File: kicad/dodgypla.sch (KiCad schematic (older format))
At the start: 10 parts, among them J1 PLA_Conn, J2 PAD_TCK, J3 PAD_TMS, J4 PAD_TDO, J5 PAD_TDI, U1 AMS1117, U2 XC9536XL-10VQ44C

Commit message: Converting to two-layer board for PCB manufacturing.
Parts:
- C1, C2, C3: symbol C -> device:C
- J1: symbol Conn_02x14_Counter_Clockwise -> conn:Conn_02x14_Counter_Clockwise
- J2, J3, J4, J5: symbol Conn_01x01 -> conn:Conn_01x01
- U1: footprint TO_SOT_Packages_SMD:SOT-223-3Lead_TabPin2 -> TO_SOT_Packages_SMD:SOT-223-3_TabPin2; symbol AMS1117 -> ams1117:AMS1117
- U2: symbol XC9536XL-10VQ44C -> xc9536xl-10vq44c:XC9536XL-10VQ44C
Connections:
- wire segments 14 -> 22
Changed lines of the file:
@@
-EESchema Schematic File Version 2
-LIBS:power
-LIBS:device
-LIBS:switches
-LIBS:relays
-LIBS:motors
-LIBS:transistors
-LIBS:conn
-LIBS:linear
-LIBS:regul
-LIBS:74xx
-LIBS:cmos4000
-LIBS:adc-dac
-LIBS:memory
-LIBS:xilinx
-LIBS:microcontrollers
-LIBS:dsp
-LIBS:microchip
-LIBS:analog_switches
-LIBS:motorola
-LIBS:texas
-LIBS:intel
-LIBS:audio
-LIBS:interface
-LIBS:digital-audio
-LIBS:philips
-LIBS:display
-LIBS:cypress
-LIBS:siliconi
-LIBS:opto
-LIBS:atmel
-LIBS:contrib
-LIBS:valves
-LIBS:xc9536xl-10vq44c
-LIBS:ams1117
+EESchema Schematic File Version 4
 LIBS:dodgypla-cache
-EELAYER 25 0
+EELAYER 29 0
 EELAYER END
 $Descr A4 11693 8268
@@
 Title "DodgyPLA"
 Date ""
-Rev "1"
+Rev "2"
 Comp ""
 Comment1 "Commodore 64 PLA Replacement"
-Comment2 "http://github.com/desaster/c64-dodgypla"
-Comment3 ""
+Comment2 "Heavily based on: http://github.com/desaster/c64-dodgypla"
+Comment3 "http://github.com/hackup/c64-dodgypla"
 Comment4 ""
 $EndDescr
 $Comp
-L Conn_02x14_Counter_Clockwise J1
+L conn:Conn_02x14_Counter_Clockwise J1
 U 1 1 5A0C74B0
 P 2100 4600
@@
 	2900 4000 2900 3750
 $Comp
-L +5V #PWR01
+L power:+5V #PWR01
 U 1 1 5A0C762B
 P 2900 3750
@@
 	1500 5300 1500 5700
 $Comp
-L GND #PWR02
+L power:GND #PWR02
 U 1 1 5A0C7674
 P 1500 5700
@@
 PLA_FE
 $Comp
-L Conn_01x01 J2
+L conn:Conn_01x01 J2
 U 1 1 5A0C7874
 P 10750 5300
@@
 $EndComp
 $Comp
-L Conn_01x01 J3
+L conn:Conn_01x01 J3
 U 1 1 5A0C793C
 P 10750 5600
@@
 $EndComp
 $Comp
-L Conn_01x01 J4
+L conn:Conn_01x01 J4
 U 1 1 5A0C797A
 P 10750 5900
@@
 $EndComp
 $Comp
-L Conn_01x01 J5
+L conn:Conn_01x01 J5
 U 1 1 5A0C7AB0
 P 10750 6200
@@
 	11000 4950 11000 6400
 $Comp
-L +3.3V #PWR03
+L power:+3.3V #PWR03
 U 1 1 5A0C804E
 P 3150 900
@@
 $EndComp
 $Comp
-L +5V #PWR04
+L power:+5V #PWR04
 U 1 1 5A0C80E4
 P 750 900
@@
 $EndComp
 $Comp
-L C C1
+L device:C C1
 U 1 1 5A0C8111
 P 1050 1050
@@
 $EndComp
 $Comp
-L GND #PWR05
+L power:GND #PWR05
 U 1 1 5A0C820D
 P 750 1450
@@
 $EndComp
 $Comp
-L C C2
+L device:C C2
 U 1 1 5A0C8072
 P 2850 1050
@@
 JTAG_TCK
 $Comp
-L C C3
+L device:C C3
 U 1 1 5A0C905D
 P 9600 2750
@@
 $EndComp
 $Comp
-L GND #PWR06
+L power:GND #PWR06
 U 1 1 5A0C90C1
 P 9600 2900
@@
 PLA_VA13
 $Comp
-L GND #PWR07
+L power:GND #PWR07
 U 1 1 5A0CABE7
 P 5450 5150
@@
 Only 1 bypass cap due\nto space constraints
 Wire Wire Line
-	750  900  1150 900
+	750  900  1050 900
 Connection ~ 1050 900
 Wire Wire Line
-	2750 900  3150 900
+	2750 900  2850 900
 Connection ~ 2850 900
 Wire Wire Line
 	2850 1400 2850 1200
 Wire Wire Line
-	750  1400 2850 1400
+	750  1400 1050 1400
 Wire Wire Line
 	750  1400 750  1450
@@
 Connection ~ 1050 1400
 $Comp
-L +5V #PWR08
+L power:+5V #PWR08
 U 1 1 5A0CBA4B
 P 1500 2000
@@
 $EndComp
 $Comp
-L PWR_FLAG #FLG09
+L power:PWR_FLAG #FLG09
 U 1 1 5A0CBA6C
 P 1500 2000
@@
 $EndComp
 $Comp
-L +3.3V #PWR010
+L power:+3.3V #PWR010
 U 1 1 5A0C9098
 P 9600 2600
@@
 $EndComp
 $Comp
-L GND #PWR011
+L power:GND #PWR011
 U 1 1 5A0CBEB0
 P 2000 2000
@@
 $EndComp
 $Comp
-L PWR_FLAG #FLG012
+L power:PWR_FLAG #FLG012
 U 1 1 5A0CBEE3
 P 2000 2000
@@
 $EndComp
 $Comp
-L XC9536XL-10VQ44C U2
+L xc9536xl-10vq44c:XC9536XL-10VQ44C U2
 U 1 1 5A6F8821
 P 5850 3600
@@
 NoConn ~ 4850 3300
 $Comp
-L +3V3 #PWR013
+L power:+3V3 #PWR013
 U 1 1 5A6F9301
 P 6300 2300
@@
 $EndComp
 Wire Wire Line
-	5650 2400 6300 2400
+	5650 2400 5850 2400
 Wire Wire Line
 	6300 2400 6300 2300
 Wire Wire Line
-	5450 5050 6050 5050
+	5450 5050 5650 5050
 Wire Wire Line
 	5450 5050 5450 5150
@@
 NoConn ~ 6850 2900
 $Comp
-L AMS1117 U1
+L ams1117:AMS1117 U1
 U 1 1 5A6FA036
 P 1950 900
 F 0 "U1" H 2200 750 50  0000 C CNN
 F 1 "AMS1117" H 1700 1000 50  0000 C CNN
-F 2 "TO_SOT_Packages_SMD:SOT-223-3Lead_TabPin2" H 1950 900 60  0001 C CNN
+F 2 "TO_SOT_Packages_SMD:SOT-223-3_TabPin2" H 1950 900 60  0001 C CNN
 F 3 "" H 1950 900 60  0000 C CNN
 	1    1950 900
 	1    0    0    -1
 $EndComp
+Wire Wire Line
+	1050 900  1150 900
+Wire Wire Line
+	2850 900  3150 900
+Wire Wire Line
+	1950 1400 2850 1400
+Wire Wire Line
+	1050 1400 1950 1400
+Wire Wire Line
+	5850 5050 6050 5050
+Wire Wire Line
+	5650 5050 5850 5050
+Wire Wire Line
+	5850 2400 6050 2400
+Wire Wire Line
+	6050 2400 6300 2400
 $EndSCHEMATC

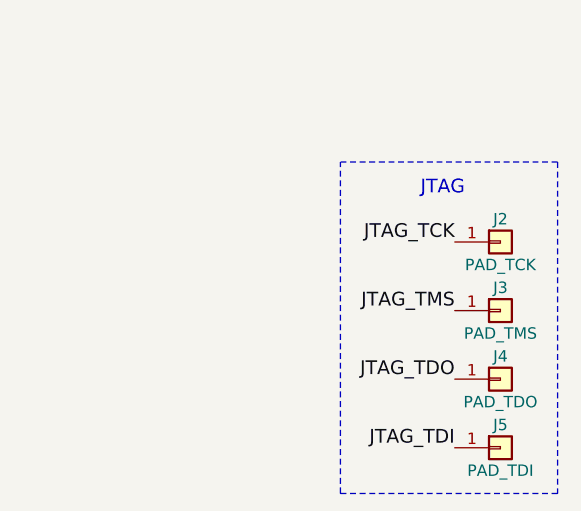
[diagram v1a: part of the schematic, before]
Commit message: Converting to two-layer board for PCB manufacturing.
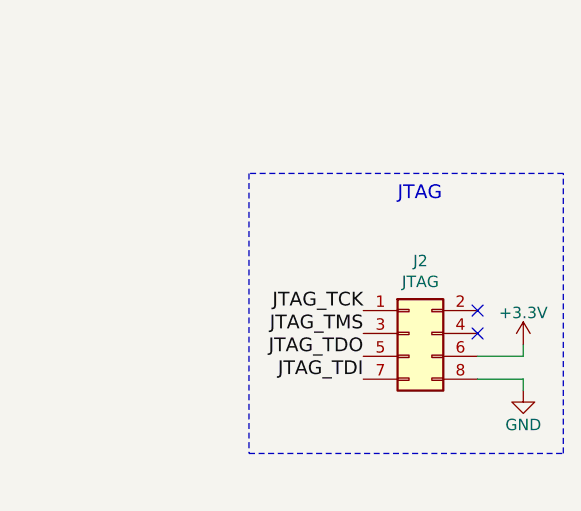
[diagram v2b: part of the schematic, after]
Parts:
- removed J2: PAD_TCK, dodgyPLA_footprints:testpad_1.6mm, symbol conn:Conn_01x01
- removed J3: PAD_TMS, dodgyPLA_footprints:testpad_1.6mm, symbol conn:Conn_01x01
- removed J4: PAD_TDO, dodgyPLA_footprints:testpad_1.6mm, symbol conn:Conn_01x01
- removed J5: PAD_TDI, dodgyPLA_footprints:testpad_1.6mm, symbol conn:Conn_01x01
- added J2: JTAG, Pin_Headers:Pin_Header_Straight_2x04_Pitch2.54mm, symbol conn:Conn_02x04_Odd_Even
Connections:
- net +3V3: now also J2.6 (Pin_6)
- net GND: now also J2.8 (Pin_8)
- net JTAG_TCK: now also J2.1 (Pin_1)
- net JTAG_TDI: now also J2.7 (Pin_7)
- net JTAG_TDO: now also J2.5 (Pin_5)
- net JTAG_TMS: now also J2.3 (Pin_3)
- no-connect marks 12 -> 14
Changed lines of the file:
@@
 Text Label 1900 4000 2    60   ~ 0
 PLA_FE
-$Comp
-L conn:Conn_01x01 J2
-U 1 1 5A0C7874
-P 10750 5300
-F 0 "J2" H 10750 5400 50  0000 C CNN
-F 1 "PAD_TCK" H 10750 5200 50  0000 C CNN
-F 2 "dodgyPLA_footprints:testpad_1.6mm" H 10750 5300 50  0001 C CNN
-F 3 "" H 10750 5300 50  0001 C CNN
-	1    10750 5300
-	1    0    0    -1
-$EndComp
-$Comp
-L conn:Conn_01x01 J3
-U 1 1 5A0C793C
-P 10750 5600
-F 0 "J3" H 10750 5700 50  0000 C CNN
-F 1 "PAD_TMS" H 10750 5500 50  0000 C CNN
-F 2 "dodgyPLA_footprints:testpad_1.6mm" H 10750 5600 50  0001 C CNN
-F 3 "" H 10750 5600 50  0001 C CNN
-	1    10750 5600
-	1    0    0    -1
-$EndComp
-$Comp
-L conn:Conn_01x01 J4
-U 1 1 5A0C797A
-P 10750 5900
-F 0 "J4" H 10750 6000 50  0000 C CNN
-F 1 "PAD_TDO" H 10750 5800 50  0000 C CNN
-F 2 "dodgyPLA_footprints:testpad_1.6mm" H 10750 5900 50  0001 C CNN
-F 3 "" H 10750 5900 50  0001 C CNN
-	1    10750 5900
-	1    0    0    -1
-$EndComp
-$Comp
-L conn:Conn_01x01 J5
-U 1 1 5A0C7AB0
-P 10750 6200
-F 0 "J5" H 10750 6300 50  0000 C CNN
-F 1 "PAD_TDI" H 10750 6100 50  0000 C CNN
-F 2 "dodgyPLA_footprints:testpad_1.6mm" H 10750 6200 50  0001 C CNN
-F 3 "" H 10750 6200 50  0001 C CNN
-	1    10750 6200
-	1    0    0    -1
-$EndComp
-Text Label 10550 5300 2    60   ~ 0
+Text Label 10150 5600 2    60   ~ 0
 JTAG_TCK
-Text Label 10550 5600 2    60   ~ 0
+Text Label 10150 5700 2    60   ~ 0
 JTAG_TMS
-Text Label 10550 5900 2    60   ~ 0
+Text Label 10150 5800 2    60   ~ 0
 JTAG_TDO
-Text Label 10550 6200 2    60   ~ 0
+Text Label 10150 5900 2    60   ~ 0
 JTAG_TDI
-Text Notes 10400 5100 0    60   ~ 0
-JTAG
-Wire Notes Line
-	11000 4950 11000 6400
 $Comp
 L power:+3.3V #PWR03
@@
 Text Label 6850 4750 0    60   ~ 0
 JTAG_TDO
-Wire Notes Line
-	11000 6400 10050 6400
-Wire Notes Line
-	10050 6400 10050 4950
-Wire Notes Line
-	10050 4950 11000 4950
 Text Label 6850 4450 0    60   ~ 0
 JTAG_TDI
@@
 Wire Wire Line
 	6050 2400 6300 2400
+NoConn ~ 10650 5600
+NoConn ~ 10650 5700
+$Comp
+L power:+3.3V #PWR0101
+U 1 1 5CA3F9DB
+P 10850 5750
+F 0 "#PWR0101" H 10850 5600 50  0001 C CNN
+F 1 "+3.3V" H 10850 5890 50  0000 C CNN
+F 2 "" H 10850 5750 50  0001 C CNN
+F 3 "" H 10850 5750 50  0001 C CNN
+	1    10850 5750
+	1    0    0    -1
+$EndComp
+$Comp
+L power:GND #PWR0102
+U 1 1 5CA40C03
+P 10850 5950
+F 0 "#PWR0102" H 10850 5700 50  0001 C CNN
+F 1 "GND" H 10850 5800 50  0000 C CNN
+F 2 "" H 10850 5950 50  0001 C CNN
+F 3 "" H 10850 5950 50  0001 C CNN
+	1    10850 5950
+	1    0    0    -1
+$EndComp
+Wire Wire Line
+	10650 5900 10850 5900
+Wire Wire Line
+	10850 5900 10850 5950
+Wire Wire Line
+	10650 5800 10850 5800
+Wire Wire Line
+	10850 5800 10850 5750
+Text Notes 10300 5125 0    60   ~ 0
+JTAG
+Wire Notes Line
+	11025 5000 9650 5000
+Wire Notes Line
+	9650 5000 9650 6225
+Wire Notes Line
+	9650 6225 11025 6225
+Wire Notes Line
+	11025 6225 11025 5000
+$Comp
+L conn:Conn_02x04_Odd_Even J2
+U 1 1 5CA48D3C
+P 10350 5700
+F 0 "J2" H 10400 6017 50  0000 C CNN
+F 1 "JTAG" H 10400 5926 50  0000 C CNN
+F 2 "Pin_Headers:Pin_Header_Straight_2x04_Pitch2.54mm" H 10350 5700 50  0001 C CNN
+F 3 "~" H 10350 5700 50  0001 C CNN
+	1    10350 5700
+	1    0    0    -1
+$EndComp
 $EndSCHEMATC

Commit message: Converting to two-layer board for PCB manufacturing.
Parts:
- C3: footprint Capacitors_SMD:C_0603 -> Capacitors_SMD:C_0805
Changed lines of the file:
@@
 F 0 "C3" H 9625 2850 50  0000 L CNN
 F 1 "0.1uF" H 9625 2650 50  0000 L CNN
-F 2 "Capacitors_SMD:C_0603" H 9638 2600 50  0001 C CNN
+F 2 "Capacitors_SMD:C_0805" H 9638 2600 50  0001 C CNN
 F 3 "" H 9600 2750 50  0001 C CNN
 	1    9600 2750

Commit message: Fixed symbol library.
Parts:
- J1: symbol conn:Conn_02x14_Counter_Clockwise -> Connector_Generic:Conn_02x14_Counter_Clockwise
- J2: symbol conn:Conn_02x04_Odd_Even -> Connector_Generic:Conn_02x04_Odd_Even
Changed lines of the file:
@@
 $EndDescr
 $Comp
-L conn:Conn_02x14_Counter_Clockwise J1
+L Connector_Generic:Conn_02x14_Counter_Clockwise J1
 U 1 1 5A0C74B0
 P 2100 4600
@@
 	11025 6225 11025 5000
 $Comp
-L conn:Conn_02x04_Odd_Even J2
+L Connector_Generic:Conn_02x04_Odd_Even J2
 U 1 1 5CA48D3C
 P 10350 5700

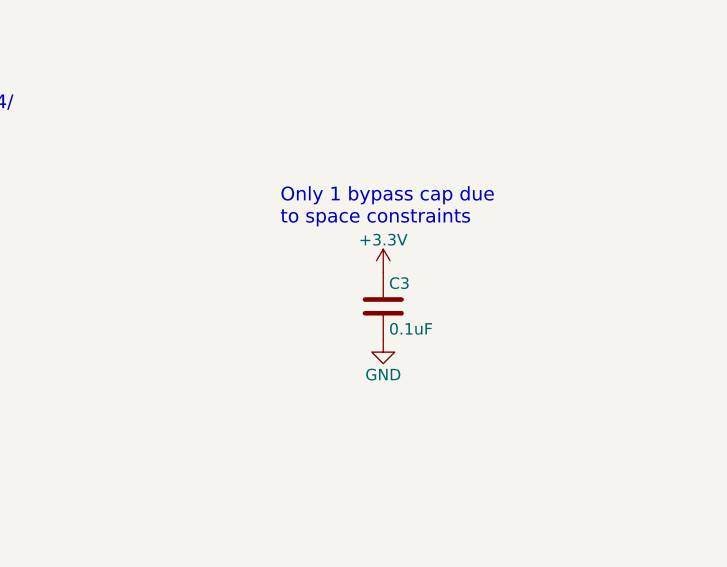
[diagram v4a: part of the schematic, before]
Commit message: Added missing bypass caps.
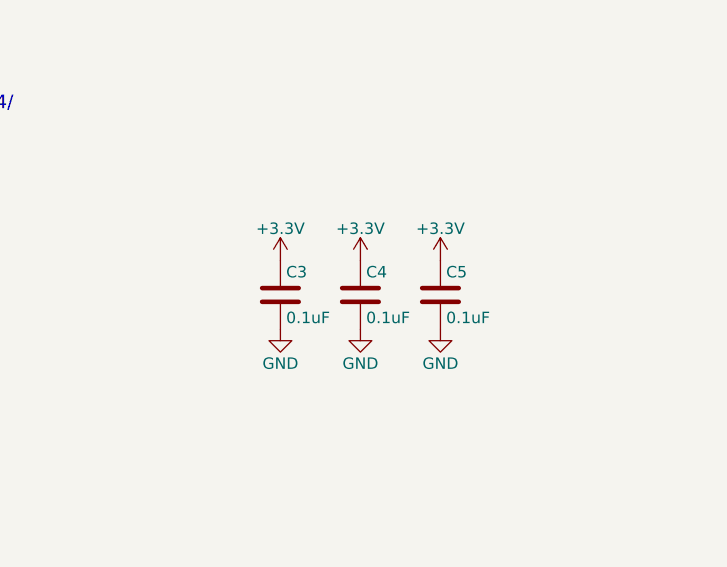
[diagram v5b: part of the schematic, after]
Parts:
- added C4, C5: 0.1uF, Capacitors_SMD:C_0805, symbol device:C
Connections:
- net +3V3: now also C4.1, C5.1
- net GND: now also C4.2, C5.2
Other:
- note removed: "Only 1 bypass cap due\nto space constraints"
- moved on the sheet: C3
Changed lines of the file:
@@
 L device:C C3
 U 1 1 5A0C905D
-P 9600 2750
-F 0 "C3" H 9625 2850 50  0000 L CNN
-F 1 "0.1uF" H 9625 2650 50  0000 L CNN
-F 2 "Capacitors_SMD:C_0805" H 9638 2600 50  0001 C CNN
-F 3 "" H 9600 2750 50  0001 C CNN
-	1    9600 2750
+P 9150 2700
+F 0 "C3" H 9175 2800 50  0000 L CNN
+F 1 "0.1uF" H 9175 2600 50  0000 L CNN
+F 2 "Capacitors_SMD:C_0805" H 9188 2550 50  0001 C CNN
+F 3 "" H 9150 2700 50  0001 C CNN
+	1    9150 2700
 	1    0    0    -1
 $EndComp
@@
 L power:GND #PWR06
 U 1 1 5A0C90C1
-P 9600 2900
-F 0 "#PWR06" H 9600 2650 50  0001 C CNN
-F 1 "GND" H 9600 2750 50  0000 C CNN
-F 2 "" H 9600 2900 50  0001 C CNN
-F 3 "" H 9600 2900 50  0001 C CNN
-	1    9600 2900
+P 9150 2850
+F 0 "#PWR06" H 9150 2600 50  0001 C CNN
+F 1 "GND" H 9150 2700 50  0000 C CNN
+F 2 "" H 9150 2850 50  0001 C CNN
+F 3 "" H 9150 2850 50  0001 C CNN
+	1    9150 2850
 	1    0    0    -1
 $EndComp
@@
 NoConn ~ 1900 4000
 NoConn ~ 2400 4900
-Text Notes 9150 2400 0    60   ~ 0
-Only 1 bypass cap due\nto space constraints
 Wire Wire Line
 	750  900  1050 900
@@
 L power:+3.3V #PWR010
 U 1 1 5A0C9098
-P 9600 2600
-F 0 "#PWR010" H 9600 2450 50  0001 C CNN
-F 1 "+3.3V" H 9600 2740 50  0000 C CNN
-F 2 "" H 9600 2600 50  0001 C CNN
-F 3 "" H 9600 2600 50  0001 C CNN
-	1    9600 2600
+P 9150 2550
+F 0 "#PWR010" H 9150 2400 50  0001 C CNN
+F 1 "+3.3V" H 9150 2690 50  0000 C CNN
+F 2 "" H 9150 2550 50  0001 C CNN
+F 3 "" H 9150 2550 50  0001 C CNN
+	1    9150 2550
 	1    0    0    -1
 $EndComp
@@
 	1    0    0    -1
 $EndComp
+$Comp
+L device:C C4
+U 1 1 5D8174F5
+P 9500 2700
+F 0 "C4" H 9525 2800 50  0000 L CNN
+F 1 "0.1uF" H 9525 2600 50  0000 L CNN
+F 2 "Capacitors_SMD:C_0805" H 9538 2550 50  0001 C CNN
+F 3 "" H 9500 2700 50  0001 C CNN
+	1    9500 2700
+	1    0    0    -1
+$EndComp
+$Comp
+L device:C C5
+U 1 1 5D817BCB
+P 9850 2700
+F 0 "C5" H 9875 2800 50  0000 L CNN
+F 1 "0.1uF" H 9875 2600 50  0000 L CNN
+F 2 "Capacitors_SMD:C_0805" H 9888 2550 50  0001 C CNN
+F 3 "" H 9850 2700 50  0001 C CNN
+	1    9850 2700
+	1    0    0    -1
+$EndComp
+$Comp
+L power:+3.3V #PWR0103
+U 1 1 5D817FDD
+P 9500 2550
+F 0 "#PWR0103" H 9500 2400 50  0001 C CNN
+F 1 "+3.3V" H 9500 2690 50  0000 C CNN
+F 2 "" H 9500 2550 50  0001 C CNN
+F 3 "" H 9500 2550 50  0001 C CNN
+	1    9500 2550
+	1    0    0    -1
+$EndComp
+$Comp
+L power:+3.3V #PWR0104
+U 1 1 5D818252
+P 9850 2550
+F 0 "#PWR0104" H 9850 2400 50  0001 C CNN
+F 1 "+3.3V" H 9850 2690 50  0000 C CNN
+F 2 "" H 9850 2550 50  0001 C CNN
+F 3 "" H 9850 2550 50  0001 C CNN
+	1    9850 2550
+	1    0    0    -1
+$EndComp
+$Comp
+L power:GND #PWR0105
+U 1 1 5D8185DB
+P 9500 2850
+F 0 "#PWR0105" H 9500 2600 50  0001 C CNN
+F 1 "GND" H 9500 2700 50  0000 C CNN
+F 2 "" H 9500 2850 50  0001 C CNN
+F 3 "" H 9500 2850 50  0001 C CNN
+	1    9500 2850
+	1    0    0    -1
+$EndComp
+$Comp
+L power:GND #PWR0106
+U 1 1 5D81886C
+P 9850 2850
+F 0 "#PWR0106" H 9850 2600 50  0001 C CNN
+F 1 "GND" H 9850 2700 50  0000 C CNN
+F 2 "" H 9850 2850 50  0001 C CNN
+F 3 "" H 9850 2850 50  0001 C CNN
+	1    9850 2850
+	1    0    0    -1
+$EndComp

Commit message: Preparing for revision 2.
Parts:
- J1: symbol Connector_Generic:Conn_02x14_Counter_Clockwise -> conn:Conn_02x14_Counter_Clockwise
- J2: symbol Connector_Generic:Conn_02x04_Odd_Even -> conn:Conn_02x04_Odd_Even
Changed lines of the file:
@@
 Sheet 1 1
 Title "DodgyPLA"
-Date ""
+Date "2019-09-20"
 Rev "2"
 Comp ""
@@
 $EndDescr
 $Comp
-L Connector_Generic:Conn_02x14_Counter_Clockwise J1
+L conn:Conn_02x14_Counter_Clockwise J1
 U 1 1 5A0C74B0
 P 2100 4600
@@
 	11025 6225 11025 5000
 $Comp
-L Connector_Generic:Conn_02x04_Odd_Even J2
+L conn:Conn_02x04_Odd_Even J2
 U 1 1 5CA48D3C
 P 10350 5700

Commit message: Use LQFP44 standard footprint.
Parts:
- C1, C2, C3, C4, C5: symbol device:C -> dodgypla-rescue:C-device
- J1: symbol conn:Conn_02x14_Counter_Clockwise -> dodgypla-rescue:Conn_02x14_Counter_Clockwise-conn
- J2: symbol conn:Conn_02x04_Odd_Even -> dodgypla-rescue:Conn_02x04_Odd_Even-conn
- U2: footprint dodgyPLA_footprints:LQFP-44_10x10mm_Pitch0.8mm -> Package_QFP:LQFP-44_10x10mm_P0.8mm
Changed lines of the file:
@@
 EESchema Schematic File Version 4
 LIBS:dodgypla-cache
-EELAYER 29 0
+EELAYER 30 0
 EELAYER END
 $Descr A4 11693 8268
@@
 Sheet 1 1
 Title "DodgyPLA"
-Date "2019-09-20"
-Rev "2"
+Date "2019-10-14"
+Rev "3"
 Comp ""
 Comment1 "Commodore 64 PLA Replacement"
@@
 $EndDescr
 $Comp
-L conn:Conn_02x14_Counter_Clockwise J1
+L dodgypla-rescue:Conn_02x14_Counter_Clockwise-conn J1
 U 1 1 5A0C74B0
 P 2100 4600
@@
 $EndComp
 $Comp
-L device:C C1
+L dodgypla-rescue:C-device C1
 U 1 1 5A0C8111
 P 1050 1050
@@
 $EndComp
 $Comp
-L device:C C2
+L dodgypla-rescue:C-device C2
 U 1 1 5A0C8072
 P 2850 1050
@@
 JTAG_TCK
 $Comp
-L device:C C3
+L dodgypla-rescue:C-device C3
 U 1 1 5A0C905D
 P 9150 2700
@@
 F 0 "U2" H 5850 3500 60  0000 C CNN
 F 1 "XC9536XL-10VQ44C" H 5850 3700 60  0000 C CNN
-F 2 "dodgyPLA_footprints:LQFP-44_10x10mm_Pitch0.8mm" H 5850 3450 60  0001 C CNN
+F 2 "Package_QFP:LQFP-44_10x10mm_P0.8mm" H 5850 3450 60  0001 C CNN
 F 3 "" H 5850 3450 60  0001 C CNN
 	1    5850 3600
@@
 	11025 6225 11025 5000
 $Comp
-L conn:Conn_02x04_Odd_Even J2
+L dodgypla-rescue:Conn_02x04_Odd_Even-conn J2
 U 1 1 5CA48D3C
 P 10350 5700
@@
 $EndComp
 $Comp
-L device:C C4
+L dodgypla-rescue:C-device C4
 U 1 1 5D8174F5
 P 9500 2700
@@
 $EndComp
 $Comp
-L device:C C5
+L dodgypla-rescue:C-device C5
 U 1 1 5D817BCB
 P 9850 2700
